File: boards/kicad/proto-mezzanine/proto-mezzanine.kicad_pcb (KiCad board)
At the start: 2 copper layers, 85 x 54 mm, 276 parts, among them J1 CONN_01X04, J1 PAD_1x1, J2 CONN_01X04, J3 CONN_01X02, J4 CONN_01X12, P1 CONN_02X20

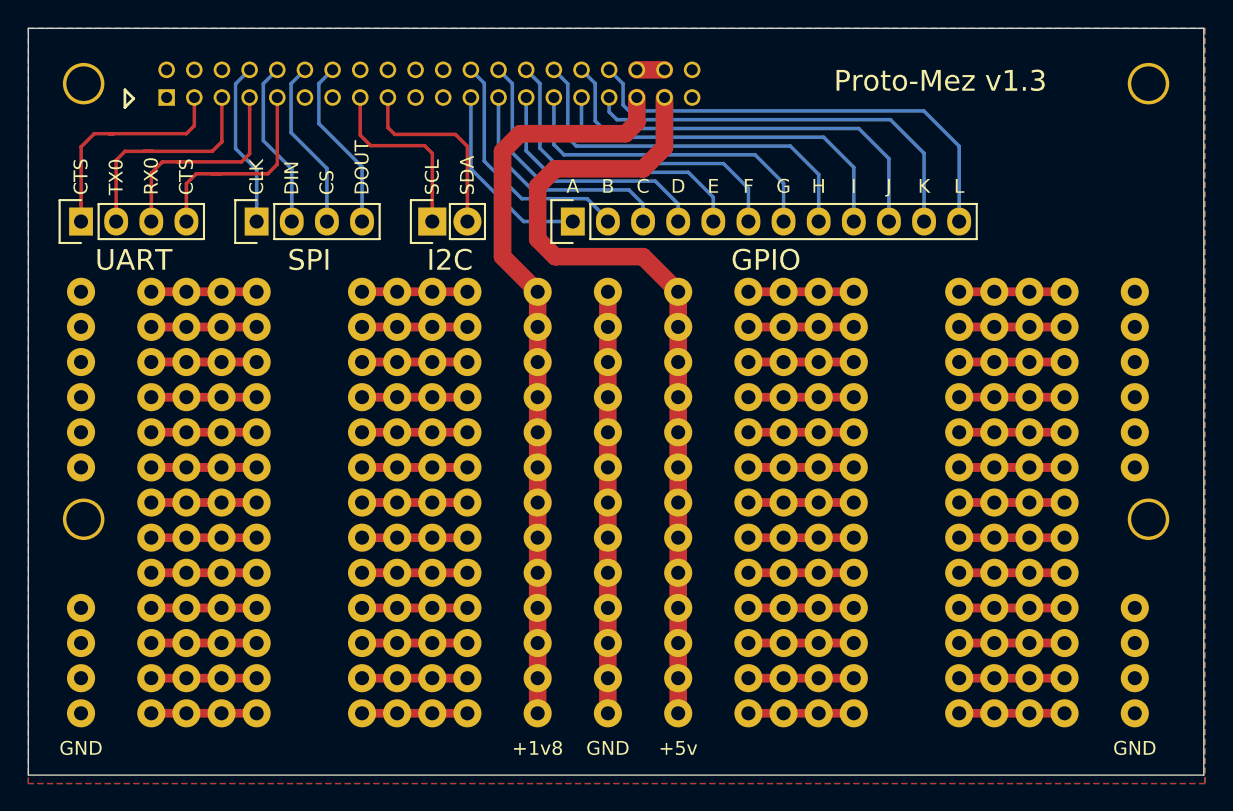
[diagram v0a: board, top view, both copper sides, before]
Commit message: Proto mezzanine updated to v1.4
Changes
- Labled i2c -> i2c0
- Removed pads from lower third to stop interference with ports on base board
- Reduced size of the board on the Y-axis

Signed-off-by: Sahaj Sarup <sahajsarup@linaro.org>
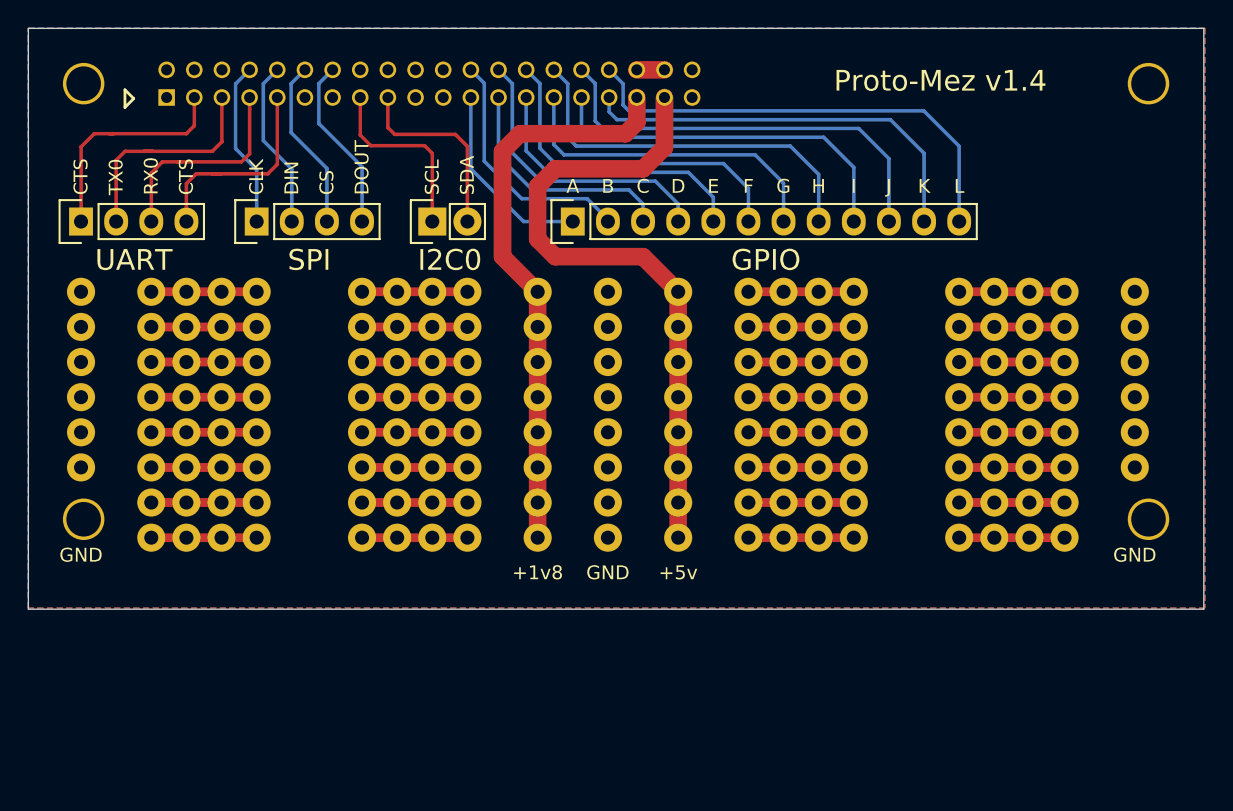
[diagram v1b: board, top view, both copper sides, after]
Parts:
- removed the J1 at (180.0, 149.5)
- removed the J1 at (180.0, 147.0)
- removed the J1 at (152.1, 149.5)
- removed the J1 at (159.7, 139.4)
- removed the J1 at (169.8, 147.0)
- removed the J1 at (174.9, 147.0)
- removed the J1 at (174.9, 144.4)
- removed the J1 at (136.8, 149.5)
- removed the J1 at (152.1, 139.4)
- removed the J1 at (157.2, 149.5)
- removed the J1 at (152.1, 147.0)
- removed the J1 at (136.8, 141.9)
- removed the J1 at (154.6, 144.4)
- removed the J1 at (157.2, 139.4)
- removed the J1 at (167.3, 149.5)
- removed the J1 at (154.6, 147.0)
- removed the J1 at (136.8, 139.4)
- removed the J1 at (167.3, 144.4)
- removed the J1 at (172.4, 141.9)
- removed the J1 at (169.8, 144.4)
- removed the J1 at (154.6, 139.4)
- removed the J1 at (136.8, 144.4)
- removed the J1 at (172.4, 139.4)
- removed the J1 at (167.3, 139.4)
- removed the J1 at (154.6, 141.9)
- removed the J1 at (172.4, 144.4)
- removed the J1 at (136.8, 147.0)
- removed the J1 at (169.8, 149.5)
- removed the J1 at (174.9, 149.5)
- removed the J1 at (154.6, 149.5)
- removed the J1 at (172.4, 147.0)
- removed the J1 at (131.8, 144.4)
- removed the J1 at (129.2, 141.9)
- removed the J1 at (131.8, 149.5)
- removed the J1 at (131.8, 147.0)
- removed the J1 at (129.2, 147.0)
- removed the J1 at (131.8, 141.9)
- removed the J1 at (129.2, 144.4)
- removed the J1 at (124.1, 144.4)
- removed the J1 at (124.1, 141.9)
- removed the J1 at (124.1, 149.5)
- removed the J1 at (131.8, 139.4)
- removed the J1 at (124.1, 139.4)
- removed the J1 at (129.2, 149.5)
- removed the J1 at (124.1, 147.0)
- removed the J1 at (126.7, 144.4)
- removed the J1 at (129.2, 139.4)
- removed the J1 at (126.7, 147.0)
- removed the J1 at (126.7, 139.4)
- removed the J1 at (126.7, 141.9)
- removed the J1 at (126.7, 149.5)
- removed the J1 at (147.0, 149.5)
- removed the J1 at (116.5, 139.4)
- removed the J1 at (147.0, 139.4)
- removed the J1 at (108.9, 139.4)
- removed the J1 at (114.0, 139.4)
- removed the J1 at (147.0, 144.4)
- removed the J1 at (111.4, 139.4)
- removed the J1 at (116.5, 144.4)
- removed the J1 at (116.5, 141.9)
- removed the J1 at (114.0, 141.9)
- removed the J1 at (108.9, 144.4)
- removed the J1 at (114.0, 144.4)
- removed the J1 at (108.9, 141.9)
- removed the J1 at (111.4, 141.9)
- removed the J1 at (111.4, 144.4)
- removed the J1 at (116.5, 147.0)
- removed the J1 at (147.0, 141.9)
- removed the J1 at (108.9, 147.0)
- removed the J1 at (114.0, 147.0)
- removed the J1 at (111.4, 147.0)
- removed the J1 at (108.9, 149.5)
- removed the J1 at (114.0, 149.5)
- removed the J1 at (116.5, 149.5)
- removed the J1 at (111.4, 149.5)
- removed the J1 at (147.0, 147.0)
- removed the J1 at (141.9, 149.5)
- removed the J1 at (141.9, 144.4)
- removed the J1 at (141.9, 147.0)
- removed the J1 at (141.9, 141.9)
- removed the J1 at (141.9, 139.4)
- removed the J1 at (103.8, 147.0)
- removed the J1 at (103.8, 144.4)
- removed the J1 at (103.8, 149.5)
- removed the J1 at (103.8, 141.9)
- removed the J1 at (159.7, 144.4)
- removed the J1 at (169.8, 139.4)
- removed the J1 at (169.8, 141.9)
- removed the J1 at (174.9, 141.9)
- removed the J1 at (167.3, 147.0)
- removed the J1 at (157.2, 141.9)
- removed the J1 at (172.4, 149.5)
- removed the J1 at (159.7, 149.5)
- removed the J1 at (159.7, 147.0)
- removed the J1 at (157.2, 147.0)
- removed the J1 at (180.0, 144.4)
- removed the J1 at (159.7, 141.9)
- removed the J1 at (157.2, 144.4)
- removed the J1 at (152.1, 144.4)
- removed the J1 at (167.3, 141.9)
- removed the J1 at (152.1, 141.9)
- removed the J1 at (180.0, 141.9)
- removed the J1 at (174.9, 139.4)
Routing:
- net (no net): track 396.2 -> 243.8 mm
- net GND: track 30.5 -> 0.00 mm
- net +5V: track 60.0 -> 47.3 mm
- net +1V8: track 54.1 -> 41.4 mm
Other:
- board size 85 x 54 mm -> 85 x 42 mm
- board text added: "I2C0"
- board text added: "Proto-Mez v1.4"
- board text removed: "I2C"
- board text removed: "Proto-Mez v1.3"
